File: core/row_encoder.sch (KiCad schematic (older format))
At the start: 3 parts

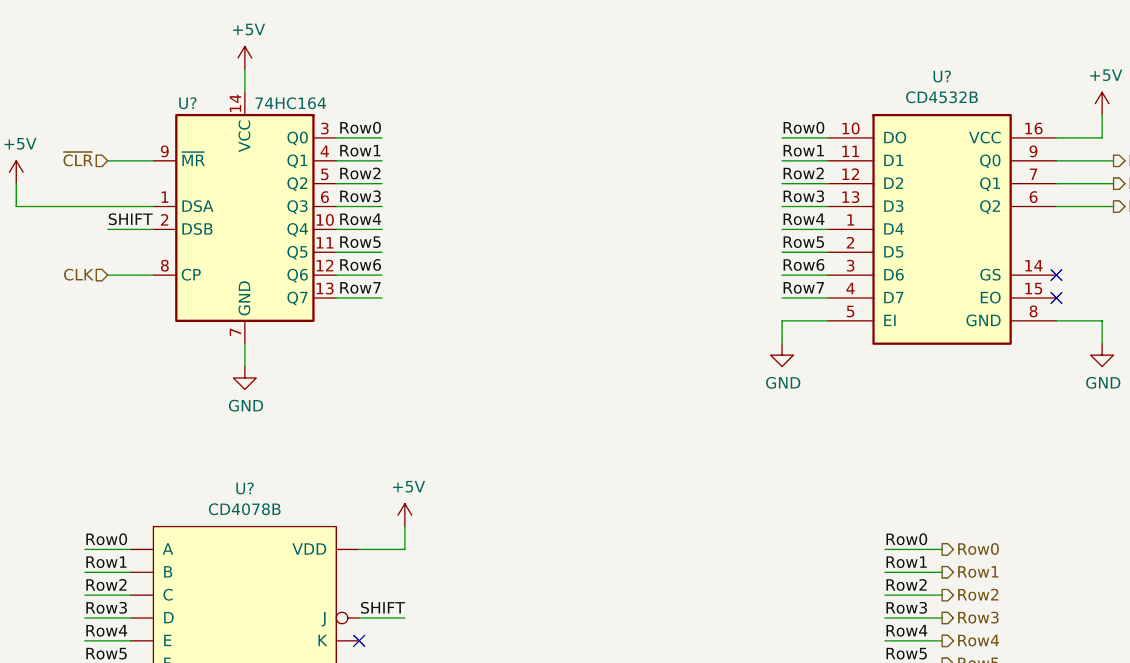
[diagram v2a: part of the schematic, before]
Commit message: Fixed ERC errors and initially populated board
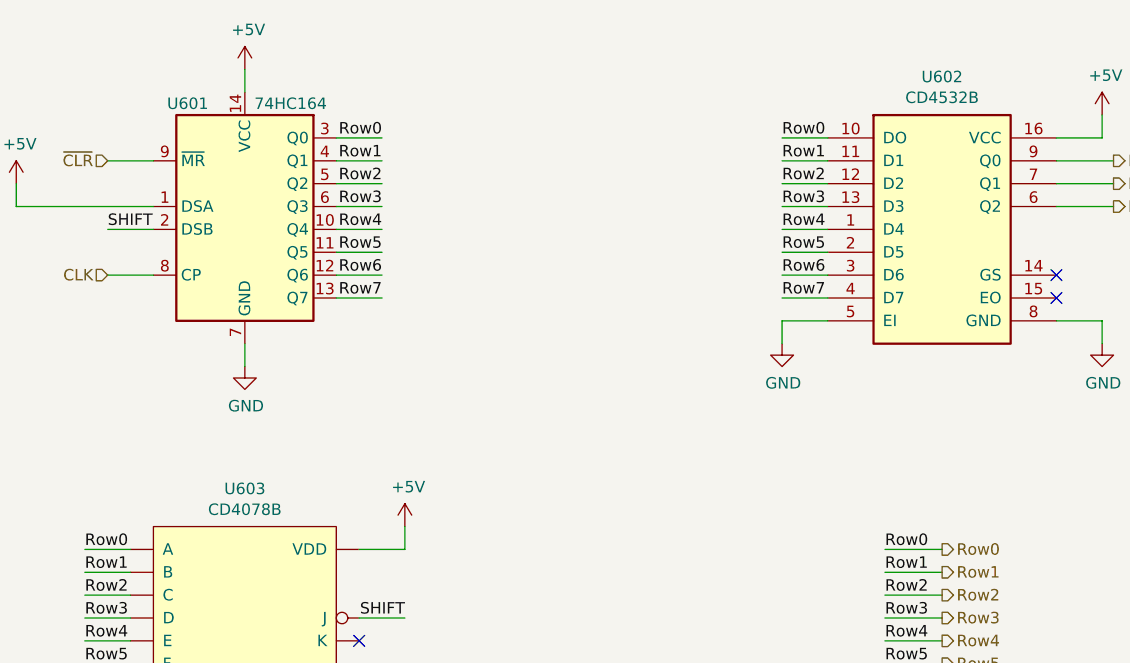
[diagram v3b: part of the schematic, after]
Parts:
- U601: renamed from U?; footprint (none) -> Package_SO:SOIC-14_3.9x8.7mm_P1.27mm
- U602: renamed from U?; footprint Package_SO:SOIC-14_3.9x8.7mm_P1.27mm -> Package_SO:SOIC-16_3.9x9.9mm_P1.27mm
- gave numbers to parts that had none: 1
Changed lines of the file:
@@
 Row7
 $Comp
-L power:GND #PWR?
+L power:GND #PWR0604
 U 1 1 5DC689CF
 P 6900 3200
-F 0 "#PWR?" H 6900 2950 50  0001 C CNN
+F 0 "#PWR0604" H 6900 2950 50  0001 C CNN
 F 1 "GND" H 6905 3027 50  0000 C CNN
 F 2 "" H 6900 3200 50  0001 C CNN
@@
 $EndComp
 $Comp
-L power:GND #PWR?
+L power:GND #PWR0605
 U 1 1 5DC68E3B
 P 8300 3200
-F 0 "#PWR?" H 8300 2950 50  0001 C CNN
+F 0 "#PWR0605" H 8300 2950 50  0001 C CNN
 F 1 "GND" H 8305 3027 50  0000 C CNN
 F 2 "" H 8300 3200 50  0001 C CNN
@@
 	6900 3100 7100 3100
 $Comp
-L power:+5V #PWR?
+L power:+5V #PWR0602
 U 1 1 5DC6EC01
 P 8300 2200
-F 0 "#PWR?" H 8300 2050 50  0001 C CNN
+F 0 "#PWR0602" H 8300 2050 50  0001 C CNN
 F 1 "+5V" H 8315 2373 50  0000 C CNN
 F 2 "" H 8300 2200 50  0001 C CNN
@@
 	8300 2300 8300 2200
 $Comp
-L 74xx:74HC164 U?
+L 74xx:74HC164 U601
 U 1 1 5DC71EBB
 P 4550 2600
-F 0 "U?" H 4300 3050 50  0000 C CNN
+F 0 "U601" H 4300 3050 50  0000 C CNN
 F 1 "74HC164" H 4750 3050 50  0000 C CNN
-F 2 "" H 5450 2300 50  0001 C CNN
+F 2 "Package_SO:SOIC-14_3.9x8.7mm_P1.27mm" H 5450 2300 50  0001 C CNN
 F 3 "https://assets.nexperia.com/documents/data-sheet/74HC_HCT164.pdf" H 5450 2300 50  0001 C CNN
 	1    4550 2600
@@
 $EndComp
 $Comp
-L power:+5V #PWR?
+L power:+5V #PWR0601
 U 1 1 5DC744BA
 P 4550 2000
-F 0 "#PWR?" H 4550 1850 50  0001 C CNN
+F 0 "#PWR0601" H 4550 1850 50  0001 C CNN
 F 1 "+5V" H 4565 2173 50  0000 C CNN
 F 2 "" H 4550 2000 50  0001 C CNN
@@
 $EndComp
 $Comp
-L power:GND #PWR?
+L power:GND #PWR0606
 U 1 1 5DC74883
 P 4550 3300
-F 0 "#PWR?" H 4550 3050 50  0001 C CNN
+F 0 "#PWR0606" H 4550 3050 50  0001 C CNN
 F 1 "GND" H 4555 3127 50  0000 C CNN
 F 2 "" H 4550 3300 50  0001 C CNN
@@
 	4150 2400 3950 2400
 $Comp
-L keyboard_project:CD4078B U?
+L keyboard_project:CD4078B U603
 U 1 1 5DCCD170
 P 4550 4450
-F 0 "U?" H 4550 5065 50  0000 C CNN
+F 0 "U603" H 4550 5065 50  0000 C CNN
 F 1 "CD4078B" H 4550 4974 50  0000 C CNN
 F 2 "Package_SO:SOIC-14_3.9x8.7mm_P1.27mm" H 4550 3850 50  0001 C CNN
@@
 	5050 4800 5250 4800
 $Comp
-L power:+5V #PWR?
+L power:+5V #PWR0607
 U 1 1 5DCED549
 P 5250 4000
-F 0 "#PWR?" H 5250 3850 50  0001 C CNN
+F 0 "#PWR0607" H 5250 3850 50  0001 C CNN
 F 1 "+5V" H 5265 4173 50  0000 C CNN
 F 2 "" H 5250 4000 50  0001 C CNN
@@
 $EndComp
 $Comp
-L power:GND #PWR?
+L power:GND #PWR0609
 U 1 1 5DCF0662
 P 5250 4900
-F 0 "#PWR?" H 5250 4650 50  0001 C CNN
+F 0 "#PWR0609" H 5250 4650 50  0001 C CNN
 F 1 "GND" H 5255 4727 50  0000 C CNN
 F 2 "" H 5250 4900 50  0001 C CNN
@@
 	3850 4800 3850 4900
 $Comp
-L power:GND #PWR?
+L power:GND #PWR0608
 U 1 1 5DCF9F09
 P 3850 4900
-F 0 "#PWR?" H 3850 4650 50  0001 C CNN
+F 0 "#PWR0608" H 3850 4650 50  0001 C CNN
 F 1 "GND" H 3855 4727 50  0000 C CNN
 F 2 "" H 3850 4900 50  0001 C CNN
@@
 	3550 2600 3550 2500
 $Comp
-L power:+5V #PWR?
+L power:+5V #PWR0603
 U 1 1 5DD01300
 P 3550 2500
-F 0 "#PWR?" H 3550 2350 50  0001 C CNN
+F 0 "#PWR0603" H 3550 2350 50  0001 C CNN
 F 1 "+5V" H 3565 2673 50  0000 C CNN
 F 2 "" H 3550 2500 50  0001 C CNN
@@
 SHIFT
 $Comp
-L keyboard_project:CD4532B U?
+L keyboard_project:CD4532B U602
 U 1 1 5DD166F6
 P 7600 2700
-F 0 "U?" H 7600 3367 50  0000 C CNN
+F 0 "U602" H 7600 3367 50  0000 C CNN
 F 1 "CD4532B" H 7600 3276 50  0000 C CNN
-F 2 "Package_SO:SOIC-14_3.9x8.7mm_P1.27mm" H 7650 1900 50  0001 C CNN
+F 2 "Package_SO:SOIC-16_3.9x9.9mm_P1.27mm" H 7650 1900 50  0001 C CNN
 F 3 "https://www.ti.com/lit/ds/symlink/cd4532b.pdf" H 7600 2700 50  0001 C CNN
 	1    7600 2700
